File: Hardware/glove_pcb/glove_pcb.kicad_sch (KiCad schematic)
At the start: 0 parts

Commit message: More work on motor driver connection
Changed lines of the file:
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@@
 (kicad_sch (version 20230121) (generator eeschema)
   (paper "A4")
-  (sheet (at 54.61 55.88) (size 43.18 31.75) (fields_autoplaced)
+  (sheet (at 50.8 50.8) (size 50.8 38.1) (fields_autoplaced)
     (stroke (width 0.1524) (type solid))
     (fill (color 0 0 0 0.0000))
-    (property "Sheetname" "Power" (at 54.61 55.1684 0)
+    (property "Sheetname" "Power" (at 50.8 50.0884 0)
       (effects (font (size 1.27 1.27)) (justify left bottom))
     )
-    (property "Sheetfile" "power.kicad_sch" (at 54.61 88.2146 0)
+    (property "Sheetfile" "power.kicad_sch" (at 50.8 89.4846 0)
       (effects (font (size 1.27 1.27)) (justify left top))
     )
@@
     )
   )
-  (sheet (at 114.3 58.42) (size 38.1 34.29) (fields_autoplaced)
+  (sheet (at 114.3 50.8) (size 50.8 38.1) (fields_autoplaced)
     (stroke (width 0.1524) (type solid))
     (fill (color 0 0 0 0.0000))
-    (property "Sheetname" "Flex" (at 114.3 57.7084 0)
+    (property "Sheetname" "Flex" (at 114.3 50.0884 0)
       (effects (font (size 1.27 1.27)) (justify left bottom))
     )
-    (property "Sheetfile" "flex.kicad_sch" (at 114.3 93.2946 0)
+    (property "Sheetfile" "flex.kicad_sch" (at 114.3 89.4846 0)
       (effects (font (size 1.27 1.27)) (justify left top))
     )
@@
     )
   )
-  (sheet (at 176.53 60.96) (size 38.1 35.56) (fields_autoplaced)
+  (sheet (at 177.8 50.8) (size 50.8 38.1) (fields_autoplaced)
     (stroke (width 0.1524) (type solid))
     (fill (color 0 0 0 0.0000))
-    (property "Sheetname" "Motor" (at 176.53 60.2484 0)
+    (property "Sheetname" "Motor" (at 177.8 50.0884 0)
       (effects (font (size 1.27 1.27)) (justify left bottom))
     )
-    (property "Sheetfile" "motor.kicad_sch" (at 176.53 97.1046 0)
+    (property "Sheetfile" "motor.kicad_sch" (at 177.8 89.4846 0)
       (effects (font (size 1.27 1.27)) (justify left top))
     )

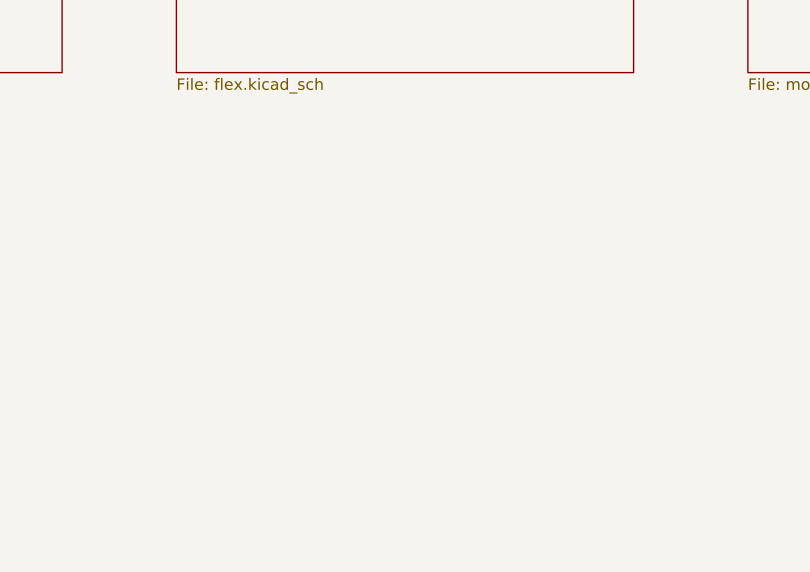
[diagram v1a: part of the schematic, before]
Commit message: Replace offboard components with connectors, add uC, add example mux, fix motor wiring
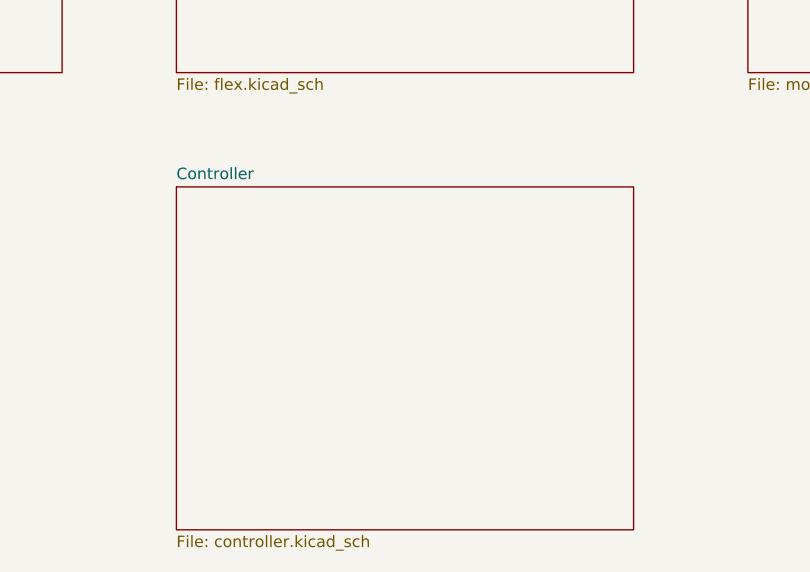
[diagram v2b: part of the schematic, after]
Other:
- added sheet Controller (controller.kicad_sch)
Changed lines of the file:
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@@
+    )
+  )
+  (sheet (at 114.3 101.6) (size 50.8 38.1) (fields_autoplaced)
+    (stroke (width 0.1524) (type solid))
+    (fill (color 0 0 0 0.0000))
+    (property "Sheetname" "Controller" (at 114.3 100.8884 0)
+      (effects (font (size 1.27 1.27)) (justify left bottom))
+    )
+    (property "Sheetfile" "controller.kicad_sch" (at 114.3 140.2846 0)
+      (effects (font (size 1.27 1.27)) (justify left top))
+    )
+    (instances
+      (project "glove_pcb"
+        (path "/747ff5f3-d342-40b0-8e4e-75b3a3063e75" (page "5"))
+      )
     )
   )

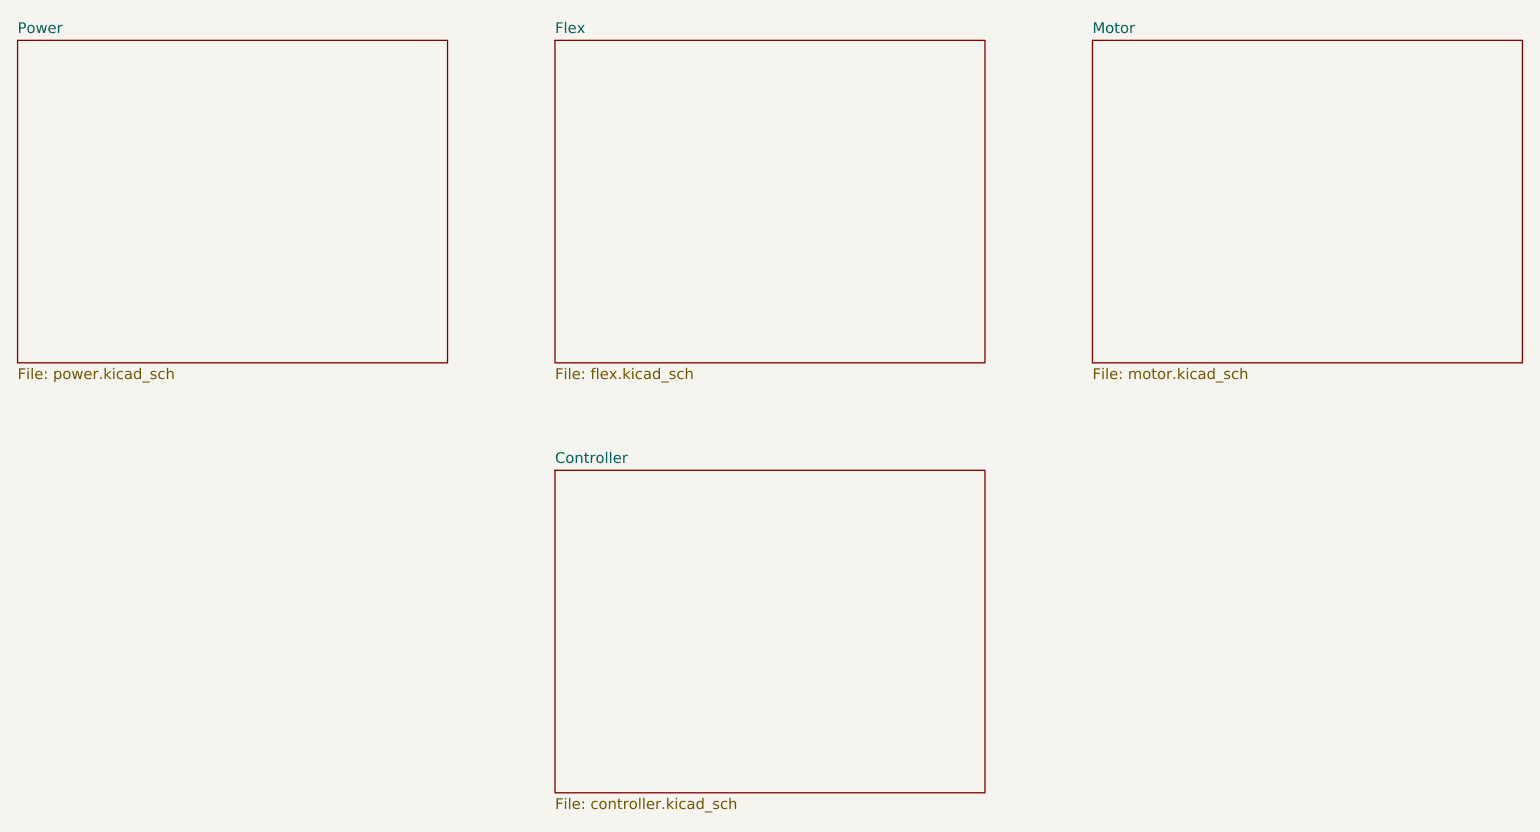
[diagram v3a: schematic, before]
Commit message: Finish schematic
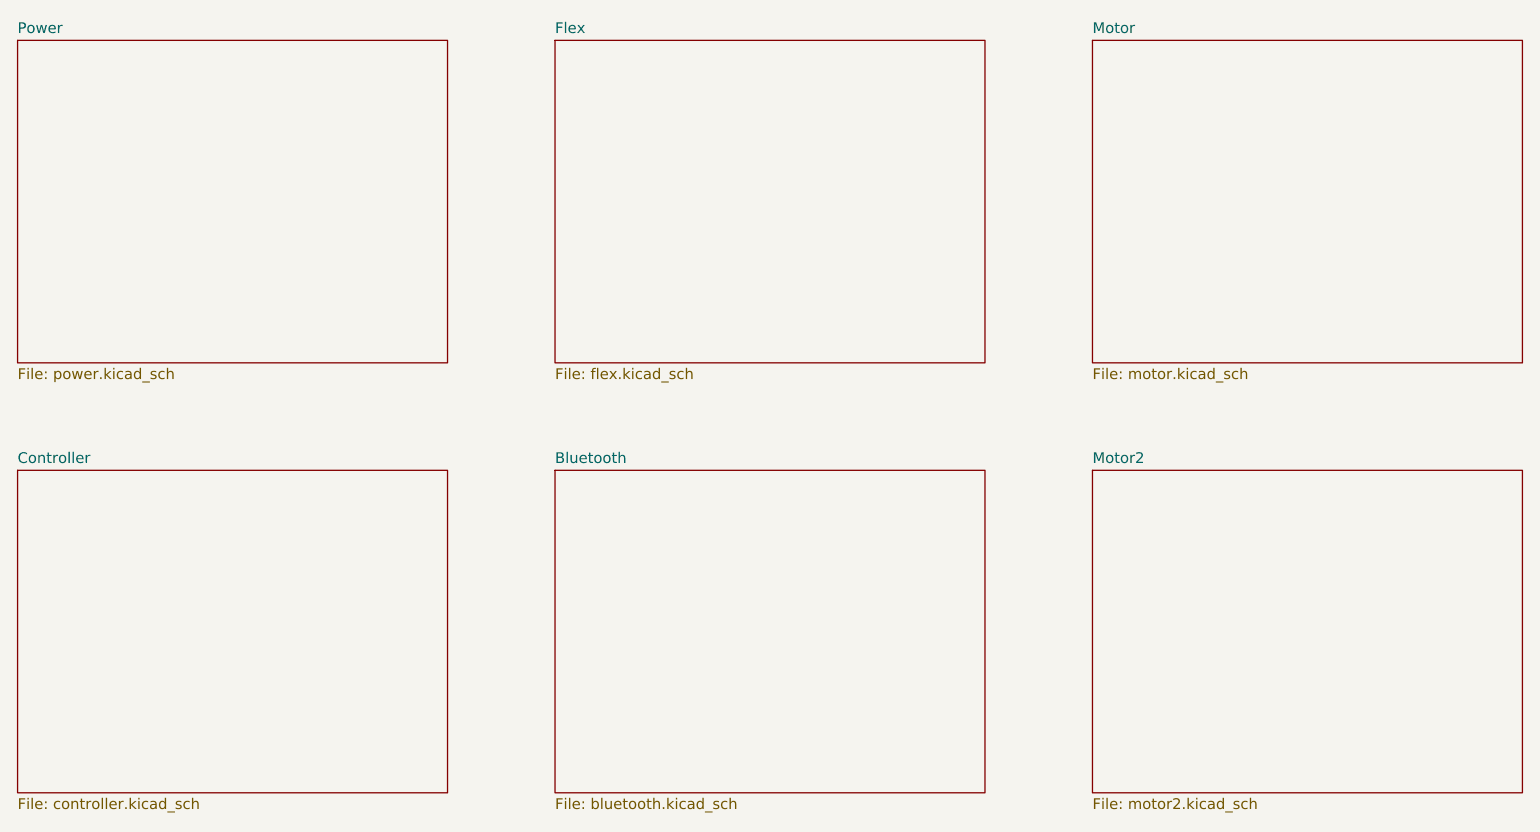
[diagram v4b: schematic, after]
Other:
- added sheet Bluetooth (bluetooth.kicad_sch)
- added sheet Motor2 (motor2.kicad_sch)
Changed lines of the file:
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@@
 (kicad_sch (version 20230121) (generator eeschema)
   (paper "USLetter")
+  (sheet (at 177.8 101.6) (size 50.8 38.1) (fields_autoplaced)
+    (stroke (width 0.1524) (type solid))
+    (fill (color 0 0 0 0.0000))
+    (property "Sheetname" "Motor2" (at 177.8 100.8884 0)
+      (effects (font (size 1.27 1.27)) (justify left bottom))
+    )
+    (property "Sheetfile" "motor2.kicad_sch" (at 177.8 140.2846 0)
+      (effects (font (size 1.27 1.27)) (justify left top))
+    )
+    (instances
+      (project "glove_pcb"
+        (path "/747ff5f3-d342-40b0-8e4e-75b3a3063e75" (page "4"))
+      )
+    )
+  )
   (sheet (at 50.8 50.8) (size 50.8 38.1) (fields_autoplaced)
     (stroke (width 0.1524) (type solid))
@@
     (instances
       (project "glove_pcb"
-        (path "/747ff5f3-d342-40b0-8e4e-75b3a3063e75" (page "4"))
+        (path "/747ff5f3-d342-40b0-8e4e-75b3a3063e75" (page "5"))
       )
     )
@@
     (stroke (width 0.1524) (type solid))
     (fill (color 0 0 0 0.0000))
-    (property "Sheetname" "Controller" (at 114.3 100.8884 0)
+    (property "Sheetname" "Bluetooth" (at 114.3 100.8884 0)
       (effects (font (size 1.27 1.27)) (justify left bottom))
     )
-    (property "Sheetfile" "controller.kicad_sch" (at 114.3 140.2846 0)
+    (property "Sheetfile" "bluetooth.kicad_sch" (at 114.3 140.2846 0)
       (effects (font (size 1.27 1.27)) (justify left top))
     )
     (instances
       (project "glove_pcb"
-        (path "/747ff5f3-d342-40b0-8e4e-75b3a3063e75" (page "5"))
+        (path "/747ff5f3-d342-40b0-8e4e-75b3a3063e75" (page "7"))
       )
     )
+  )
+  (sheet (at 50.8 101.6) (size 50.8 38.1) (fields_autoplaced)
+    (stroke (width 0.1524) (type solid))
+    (fill (color 0 0 0 0.0000))
+    (property "Sheetname" "Controller" (at 50.8 100.8884 0)
+      (effects (font (size 1.27 1.27)) (justify left bottom))
+    )
+    (property "Sheetfile" "controller.kicad_sch" (at 50.8 140.2846 0)
+      (effects (font (size 1.27 1.27)) (justify left top))
+    )
+    (instances
+      (project "glove_pcb"
+        (path "/747ff5f3-d342-40b0-8e4e-75b3a3063e75" (page "6"))
+      )
+    )

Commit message: Add titles to pages and reannotate
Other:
- company: (none) -> COEN 490 Team 15
- title: (none) -> Hand Rehabilitation Glove Companion Board
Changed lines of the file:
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@@
 (kicad_sch (version 20230121) (generator eeschema)
   (paper "USLetter")
+  (title_block
+    (title "Hand Rehabilitation Glove Companion Board")
+    (date "2023-11-24")
+    (company "COEN 490 Team 15")
+  )
   (sheet (at 177.8 101.6) (size 50.8 38.1) (fields_autoplaced)
     (stroke (width 0.1524) (type solid))
